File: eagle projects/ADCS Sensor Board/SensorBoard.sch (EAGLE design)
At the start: 85 parts, among them J5 HDR_10_EZFET_DEBUGGER, J6 MTI-1_8428-11B1-RK-TP, Q1 BC850SMD, Q2 IRF7507TRPBF, U1 MSP430F5529IPN, U2 LMV321, U3 ADS7841E_2K5, U4 LMV321, U5 LM20BIM7X_NOPB, U6 LMV321, Y1 32.768kHz, Y2 CSTCR4M00G15L99

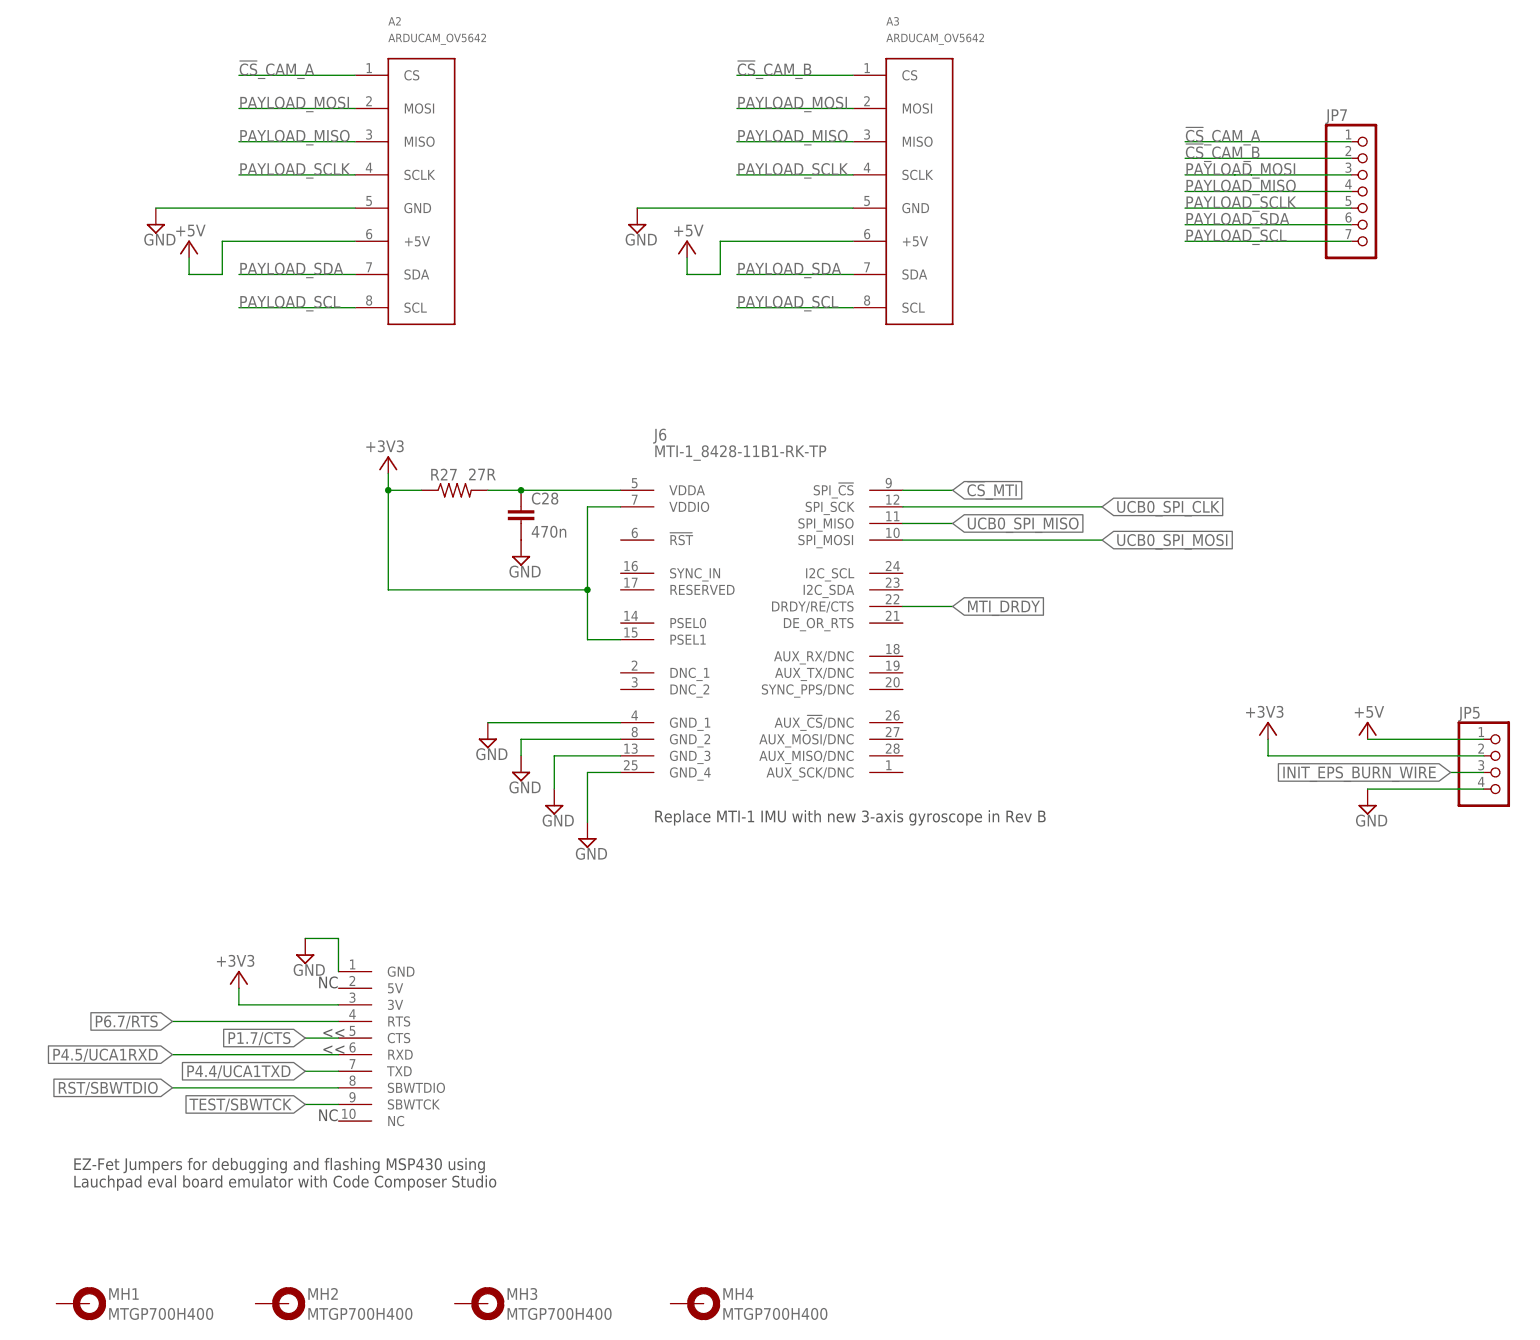
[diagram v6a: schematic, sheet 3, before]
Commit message: Laid out pinout traces
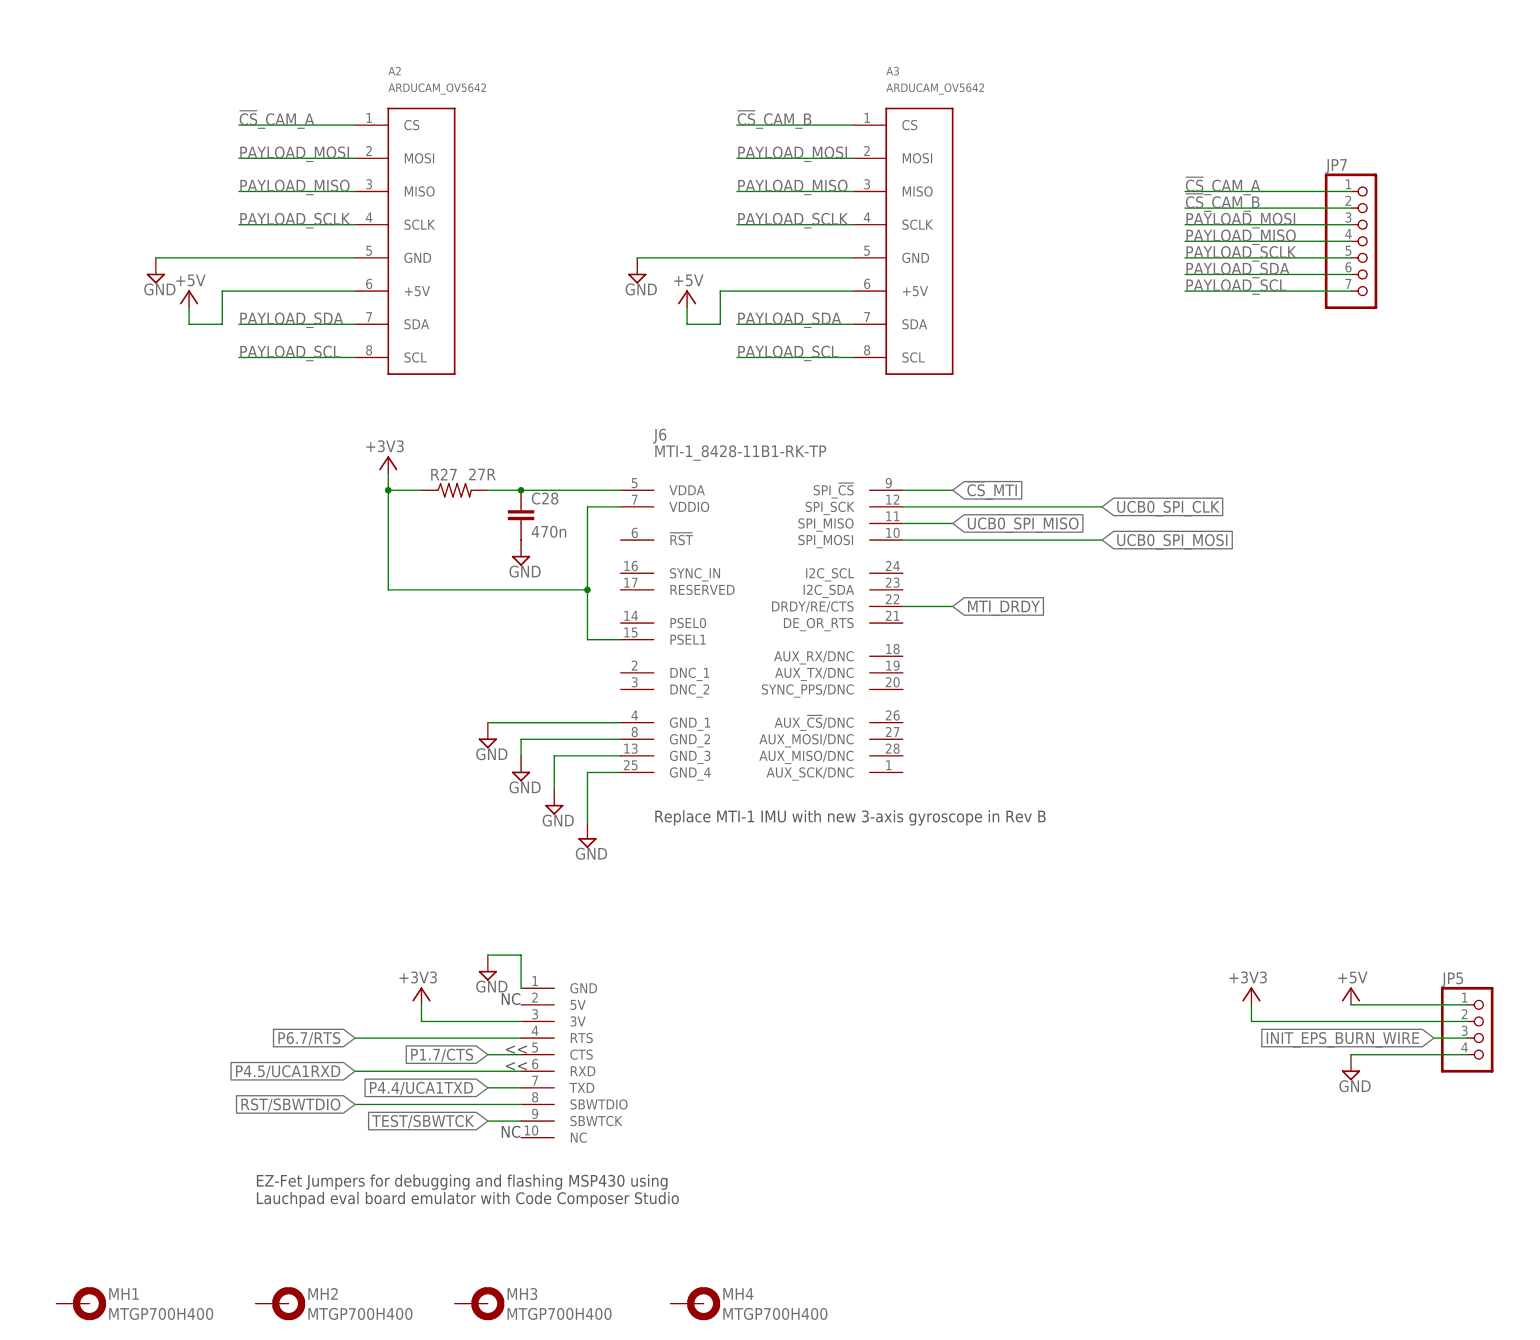
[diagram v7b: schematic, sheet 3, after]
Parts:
- JP5, JP8, JP9: device pinhead:PINHD-1X4 -> my_library:PINHD-1X4
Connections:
- removed net P2.2: U1.P2.2/TA2CLK/SMCLK
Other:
- moved on the sheet: A2, A3, C10, JP5, JP7, JP8, JP9, Q1, R2, S1, Y2
